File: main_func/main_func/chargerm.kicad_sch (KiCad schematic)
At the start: 15 parts, among them IC1 LN4056-ESOP8, J3 Battery, TEMP, Q1 Q_PMOS_GSD, SW1 SW_DPDT

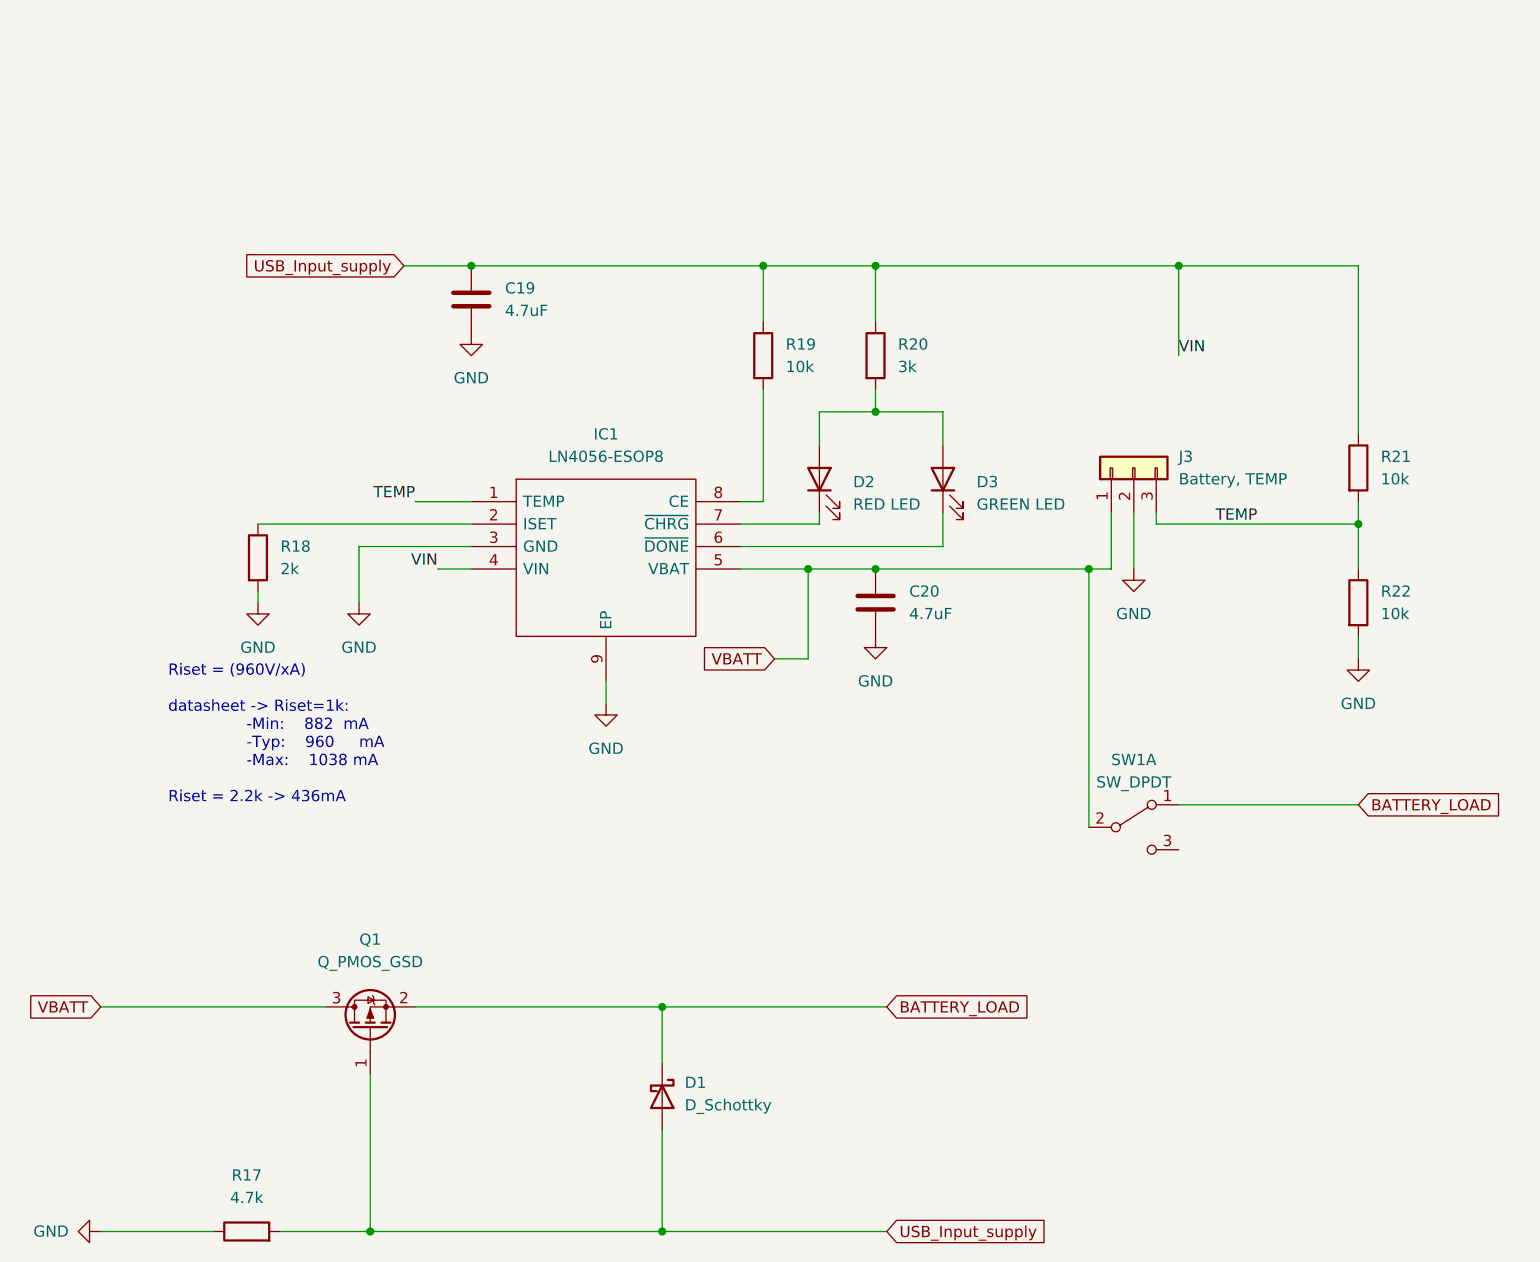
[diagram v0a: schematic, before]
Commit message: main func schematics fixed
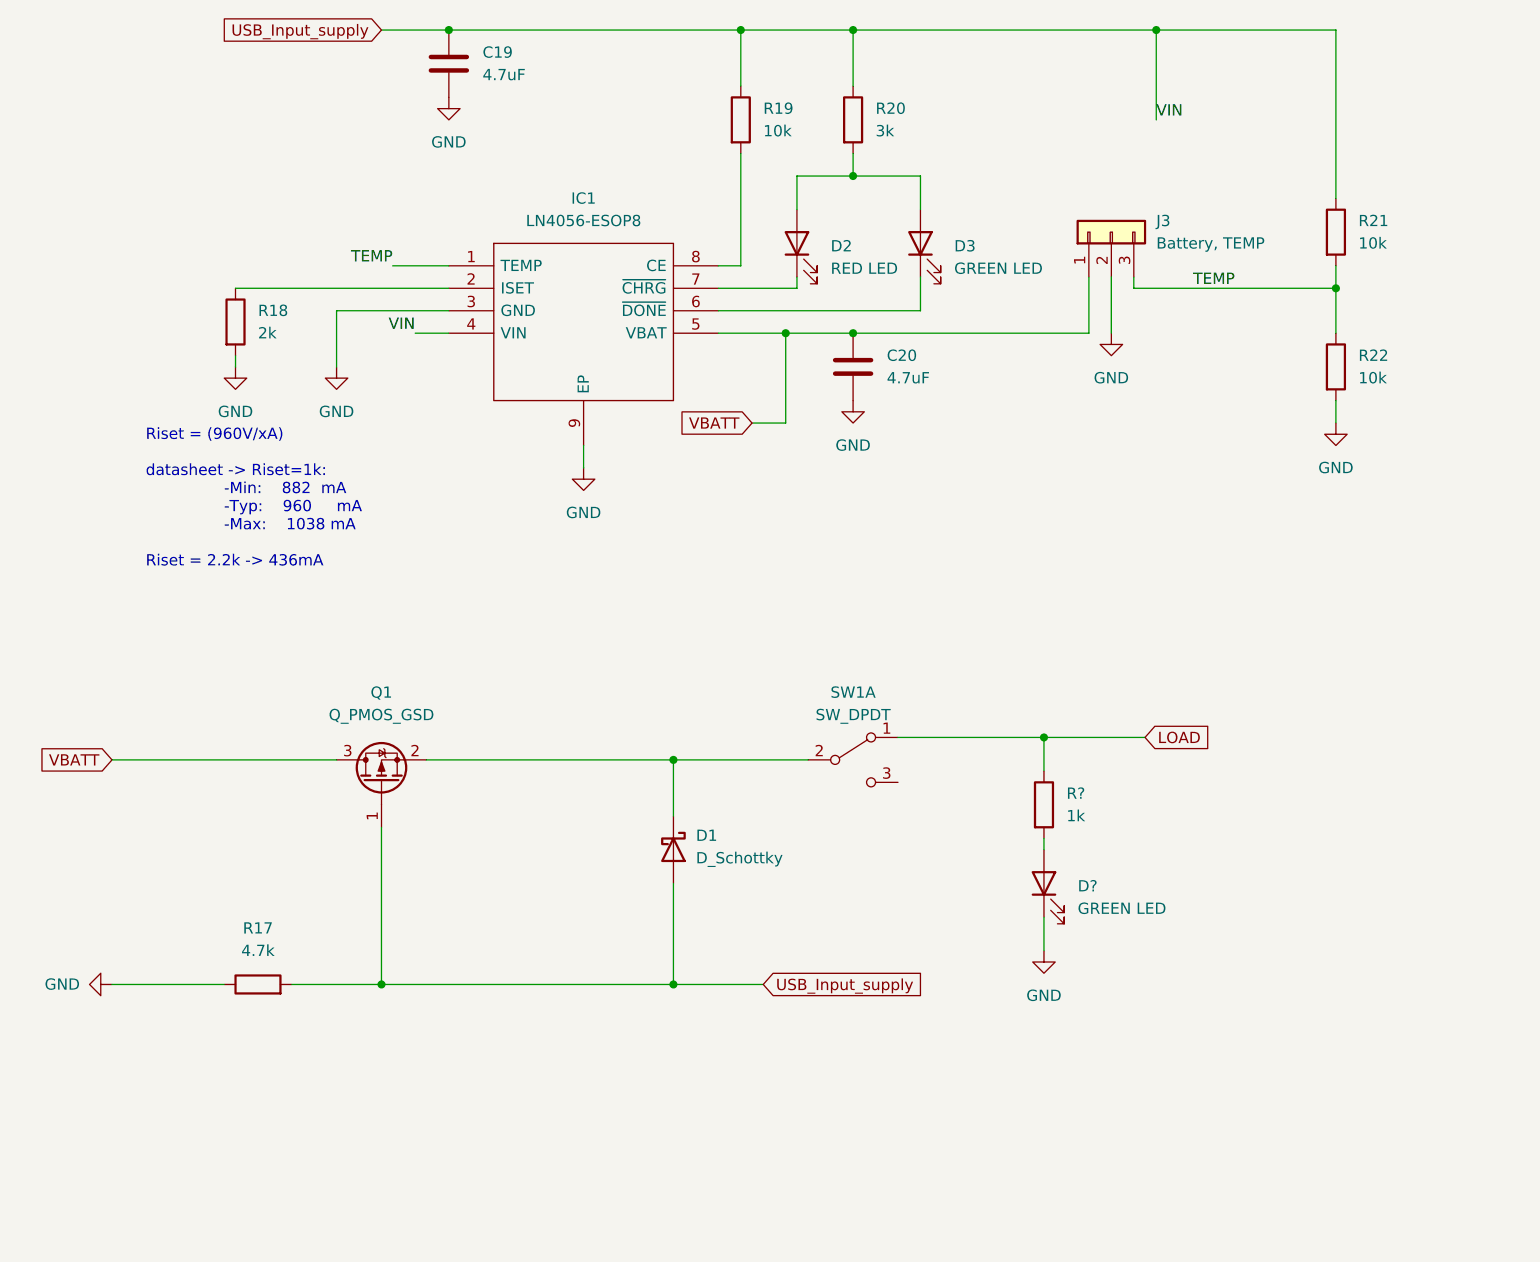
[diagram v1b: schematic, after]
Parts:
- added D?: GREEN LED, LED_SMD:LED_0805_2012Metric_Pad1.15x1.40mm_HandSolder, symbol Device:LED
- added R?: 1k, Resistor_SMD:R_0805_2012Metric_Pad1.20x1.40mm_HandSolder, symbol Device:R
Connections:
- net GND: now also D?.1 (K)
- net VBATT: no longer SW1.2 (B)
- net BATTERY_LOAD: no longer names the net of D1.1 (K), Q1.2 (S)
- net BATTERY_LOAD: now also SW1.2 (B); no longer SW1.1 (A)
- new net: D?.2 (A), R?.2
- new net LOAD: R?.1, SW1.1 (A)
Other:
- moved on the sheet: C19, C20, D1, D2, D3, IC1, J3, Q1, R17, R18, R19, R20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

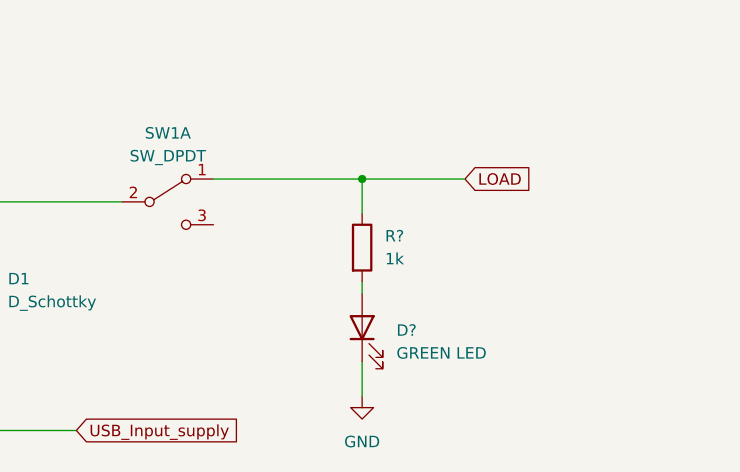
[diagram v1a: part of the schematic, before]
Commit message: fixing keyboard and pot project schematics
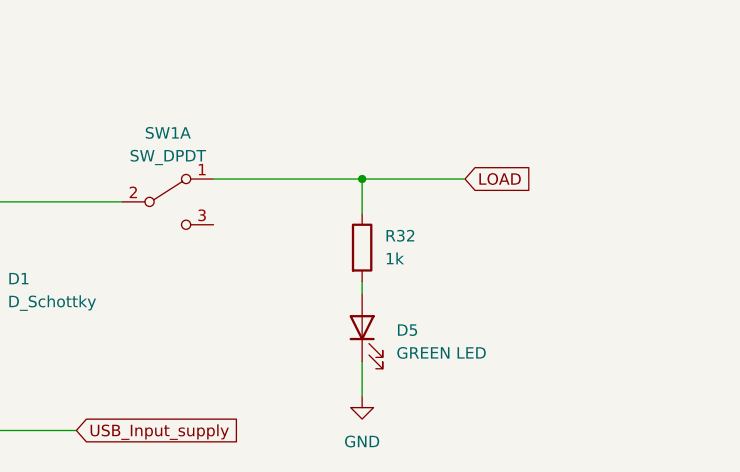
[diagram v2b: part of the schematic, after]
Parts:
- gave numbers to parts that had none: 2
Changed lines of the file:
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@@
   (symbol (lib_id "Device:LED") (at 158.75 123.19 90) (unit 1)
     (in_bom yes) (on_board yes) (fields_autoplaced)
-    (property "Reference" "D?" (id 0) (at 162.56 123.5074 90)
+    (property "Reference" "D5" (id 0) (at 162.56 123.5074 90)
       (effects (font (size 1.27 1.27)) (justify right))
     )
@@
   (symbol (lib_id "Device:R") (at 158.75 114.3 0) (unit 1)
     (in_bom yes) (on_board yes) (fields_autoplaced)
-    (property "Reference" "R?" (id 0) (at 161.29 113.0299 0)
+    (property "Reference" "R32" (id 0) (at 161.29 113.0299 0)
       (effects (font (size 1.27 1.27)) (justify left))
     )
@@
   (symbol (lib_id "power:GND") (at 158.75 130.81 0) (unit 1)
     (in_bom yes) (on_board yes) (fields_autoplaced)
-    (property "Reference" "#PWR?" (id 0) (at 158.75 137.16 0)
+    (property "Reference" "#PWR012" (id 0) (at 158.75 137.16 0)
       (effects (font (size 1.27 1.27)) hide)
     )

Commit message: main_func pcb done
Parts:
- removed D1: D_Schottky, symbol Device:D_Schottky
- added D1: FUXINSEMI DSK34 (SOD-123), Diode_SMD:D_SOD-123, symbol Diode:BAT42W-V
- C19, C20: value 4.7uF -> 4.7u
- Q1: value Q_PMOS_GSD -> CJ2301; footprint (none) -> Package_TO_SOT_SMD:SOT-23_Handsoldering
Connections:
- net USB_Input_supply: now also D1.2 (A)
- net at Q1.2 (S), SW1.2 (B): now also D1.1 (K)
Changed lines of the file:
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@@
   (junction (at 137.16 26.67) (diameter 0) (color 0 0 0 0)
   )
+  (junction (at 116.84 109.22) (diameter 0) (color 0 0 0 0)
+  )
   (junction (at 158.75 106.68) (diameter 0) (color 0 0 0 0)
   )
-  (junction (at 116.84 109.22) (diameter 0) (color 0 0 0 0)
-  )
   (junction (at 124.46 26.67) (diameter 0) (color 0 0 0 0)
   )
@@
     (stroke (width 0) (type default) (color 0 0 0 0))
   )
-  (wire (pts (xy 116.84 134.62) (xy 116.84 123.19))
+  (wire (pts (xy 116.84 121.92) (xy 116.84 134.62))
     (stroke (width 0) (type default) (color 0 0 0 0))
   )
@@
     (stroke (width 0) (type default) (color 0 0 0 0))
   )
-  (wire (pts (xy 116.84 115.57) (xy 116.84 109.22))
+  (wire (pts (xy 191.77 53.34) (xy 191.77 55.88))
+    (stroke (width 0) (type default) (color 0 0 0 0))
+  )
+  (wire (pts (xy 158.75 118.11) (xy 158.75 119.38))
+    (stroke (width 0) (type default) (color 0 0 0 0))
+  )
+  (wire (pts (xy 116.84 109.22) (xy 116.84 114.3))
+    (stroke (width 0) (type default) (color 0 0 0 0))
+  )
+  (wire (pts (xy 137.16 60.96) (xy 163.83 60.96))
+    (stroke (width 0) (type default) (color 0 0 0 0))
+  )
+  (wire (pts (xy 121.92 60.96) (xy 129.54 60.96))
+    (stroke (width 0) (type default) (color 0 0 0 0))
+  )
+  (wire (pts (xy 158.75 127) (xy 158.75 130.81))
+    (stroke (width 0) (type default) (color 0 0 0 0))
+  )
+  (wire (pts (xy 106.68 73.66) (xy 106.68 76.2))
     (stroke (width 0) (type default) (color 0 0 0 0))
   )
   (wire (pts (xy 116.84 109.22) (xy 132.08 109.22))
-    (stroke (width 0) (type default) (color 0 0 0 0))
-  )
-  (wire (pts (xy 191.77 53.34) (xy 191.77 55.88))
-    (stroke (width 0) (type default) (color 0 0 0 0))
-  )
-  (wire (pts (xy 158.75 118.11) (xy 158.75 119.38))
-    (stroke (width 0) (type default) (color 0 0 0 0))
-  )
-  (wire (pts (xy 137.16 60.96) (xy 163.83 60.96))
-    (stroke (width 0) (type default) (color 0 0 0 0))
-  )
-  (wire (pts (xy 121.92 60.96) (xy 129.54 60.96))
-    (stroke (width 0) (type default) (color 0 0 0 0))
-  )
-  (wire (pts (xy 158.75 127) (xy 158.75 130.81))
-    (stroke (width 0) (type default) (color 0 0 0 0))
-  )
-  (wire (pts (xy 106.68 73.66) (xy 106.68 76.2))
     (stroke (width 0) (type default) (color 0 0 0 0))
   )
@@
       (effects (font (size 1.27 1.27)) (justify left))
     )
-    (property "Value" "4.7uF" (id 1) (at 95.25 31.7499 0)
+    (property "Value" "4.7u" (id 1) (at 95.25 31.7499 0)
       (effects (font (size 1.27 1.27)) (justify left))
     )
@@
     (in_bom yes) (on_board yes) (fields_autoplaced)
     (property "Reference" "Q1" (id 0) (at 83.82 101.6 90))
-    (property "Value" "Q_PMOS_GSD" (id 1) (at 83.82 104.14 90))
-    (property "Footprint" "" (id 2) (at 81.28 106.68 0)
+    (property "Value" "CJ2301" (id 1) (at 83.82 104.14 90))
+    (property "Footprint" "Package_TO_SOT_SMD:SOT-23_Handsoldering" (id 2) (at 81.28 106.68 0)
       (effects (font (size 1.27 1.27)) hide)
     )
@@
       (effects (font (size 1.27 1.27)) (justify left))
     )
-    (property "Value" "4.7uF" (id 1) (at 140.97 66.0399 0)
+    (property "Value" "4.7u" (id 1) (at 140.97 66.0399 0)
       (effects (font (size 1.27 1.27)) (justify left))
     )
@@
     (pin "9")
   )
+  (symbol (lib_id "Diode:BAT42W-V") (at 116.84 118.11 270) (unit 1)
+    (in_bom yes) (on_board yes) (fields_autoplaced)
+    (property "Reference" "D1" (id 0) (at 119.38 116.5224 90)
+      (effects (font (size 1.27 1.27)) (justify left))
+    )
+    (property "Value" "FUXINSEMI DSK34 (SOD-123)" (id 1) (at 119.38 119.0624 90)
+      (effects (font (size 1.27 1.27)) (justify left))
+    )
+    (property "Footprint" "Diode_SMD:D_SOD-123" (id 2) (at 112.395 118.11 0)
+      (effects (font (size 1.27 1.27)) hide)
+    )
+    (property "Datasheet" "https://datasheet.lcsc.com/lcsc/2010271836_FUXINSEMI-DSK34_C908230.pdf" (id 3) (at 116.84 118.11 0)
+      (effects (font (size 1.27 1.27)) hide)
+    )
+    (pin "1")
+    (pin "2")
+  )
   (symbol (lib_id "Device:LED") (at 144.78 50.8 90) (unit 1)
     (in_bom yes) (on_board yes) (fields_autoplaced)
@@
       (effects (font (size 1.27 1.27)) hide)
     )
-    (pin "1")
-    (pin "2")
-  )
-  (symbol (lib_id "Device:D_Schottky") (at 116.84 119.38 270) (unit 1)
-    (in_bom yes) (on_board yes) (fields_autoplaced)
-    (property "Reference" "D1" (id 0) (at 119.38 117.7924 90)
-      (effects (font (size 1.27 1.27)) (justify left))
-    )
-    (property "Value" "D_Schottky" (id 1) (at 119.38 120.3324 90)
-      (effects (font (size 1.27 1.27)) (justify left))
-    )
-    (property "Footprint" "" (id 2) (at 116.84 119.38 0)
-      (effects (font (size 1.27 1.27)) hide)
-    )
-    (property "Datasheet" "~" (id 3) (at 116.84 119.38 0)
-      (effects (font (size 1.27 1.27)) hide)
-    )

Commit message: pcb design fixing
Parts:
- removed J3: Battery, TEMP, Connector_PinSocket_2.54mm:PinSocket_1x03_P2.54mm_Horizontal, symbol Connector_Generic:Conn_01x03
- added J5: Battery, TEMP, Connector_PinHeader_2.54mm:PinHeader_1x04_P2.54mm_Horizontal, symbol Connector:Conn_01x04_Male
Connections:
- net GND: now also J5.1 (Pin_1), J5.3 (Pin_3)
- net TEMP: now also J5.2 (Pin_2)
- net VBATT: now also J5.4 (Pin_4)
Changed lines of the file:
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@@
   (junction (at 191.77 55.88) (diameter 0) (color 0 0 0 0)
+  )
+  (wire (pts (xy 171.45 54.61) (xy 171.45 60.96))
+    (stroke (width 0) (type default) (color 0 0 0 0))
   )
   (wire (pts (xy 163.83 54.61) (xy 163.83 60.96))
@@
     (pin "2")
   )
-  (symbol (lib_id "Connector_Generic:Conn_01x03") (at 166.37 49.53 90) (unit 1)
-    (in_bom yes) (on_board yes) (fields_autoplaced)
-    (property "Reference" "J3" (id 0) (at 171.45 48.2599 90)
-      (effects (font (size 1.27 1.27)) (justify right))
-    )
-    (property "Value" "Battery, TEMP" (id 1) (at 171.45 50.7999 90)
-      (effects (font (size 1.27 1.27)) (justify right))
-    )
-    (property "Footprint" "Connector_PinSocket_2.54mm:PinSocket_1x03_P2.54mm_Horizontal" (id 2) (at 166.37 49.53 0)
-      (effects (font (size 1.27 1.27)) hide)
-    )
-    (property "Datasheet" "~" (id 3) (at 166.37 49.53 0)
-      (effects (font (size 1.27 1.27)) hide)
-    )
-    (pin "1")
-    (pin "2")
-    (pin "3")
-  )
   (symbol (lib_id "Device:LED") (at 158.75 123.19 90) (unit 1)
     (in_bom yes) (on_board yes) (fields_autoplaced)
@@
     (pin "2")
   )
+  (symbol (lib_id "Connector:Conn_01x04_Male") (at 168.91 49.53 270) (unit 1)
+    (in_bom yes) (on_board yes) (fields_autoplaced)
+    (property "Reference" "J5" (id 0) (at 167.64 44.45 90))
+    (property "Value" "Battery, TEMP" (id 1) (at 167.64 46.99 90))
+    (property "Footprint" "Connector_PinHeader_2.54mm:PinHeader_1x04_P2.54mm_Horizontal" (id 2) (at 168.91 49.53 0)
+      (effects (font (size 1.27 1.27)) hide)
+    )
+    (property "Datasheet" "~" (id 3) (at 168.91 49.53 0)
+      (effects (font (size 1.27 1.27)) hide)
+    )
+    (pin "1")
+    (pin "2")
+    (pin "3")
+    (pin "4")
+  )
   (symbol (lib_id "Device:R") (at 69.85 134.62 90) (unit 1)
     (in_bom yes) (on_board yes) (fields_autoplaced)
@@
       (effects (font (size 1.27 1.27)) hide)
     )
+    (pin "1")
+  )
+  (symbol (lib_id "power:GND") (at 171.45 60.96 0) (unit 1)
+    (in_bom yes) (on_board yes) (fields_autoplaced)
+    (property "Reference" "#PWR0106" (id 0) (at 171.45 67.31 0)
+      (effects (font (size 1.27 1.27)) hide)
+    )
+    (property "Value" "GND" (id 1) (at 171.45 66.04 0))
+    (property "Footprint" "" (id 2) (at 171.45 60.96 0)
+      (effects (font (size 1.27 1.27)) hide)
+    )
+    (property "Datasheet" "" (id 3) (at 171.45 60.96 0)
+      (effects (font (size 1.27 1.27)) hide)
+    )
